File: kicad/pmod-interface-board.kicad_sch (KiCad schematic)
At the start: 30 parts, among them J1 PMOD Connector 1, J2 PMOD Connector 2, J4 Gameboy Cart Connector, U1 74HCT541, U2 74HCT541, U3 74HC595, U4 74HC595, U5 74HC595, U6 74HC597

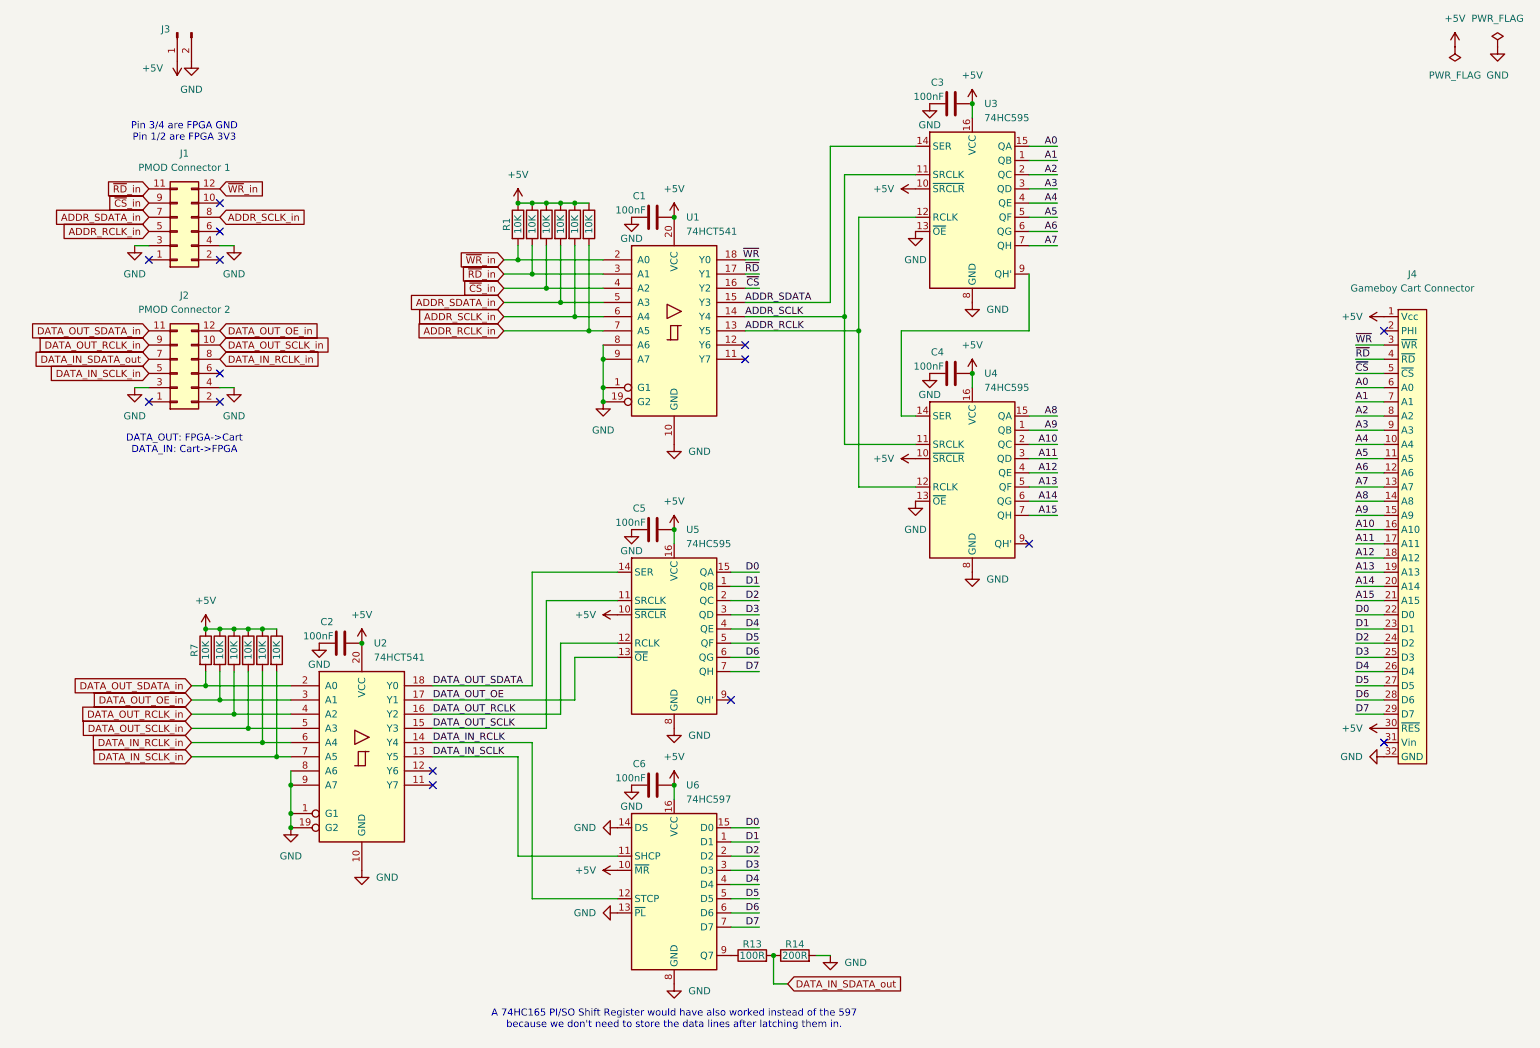
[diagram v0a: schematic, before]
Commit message: kicad: fixed faulty 597 wiring and moved pullups to +3.3v
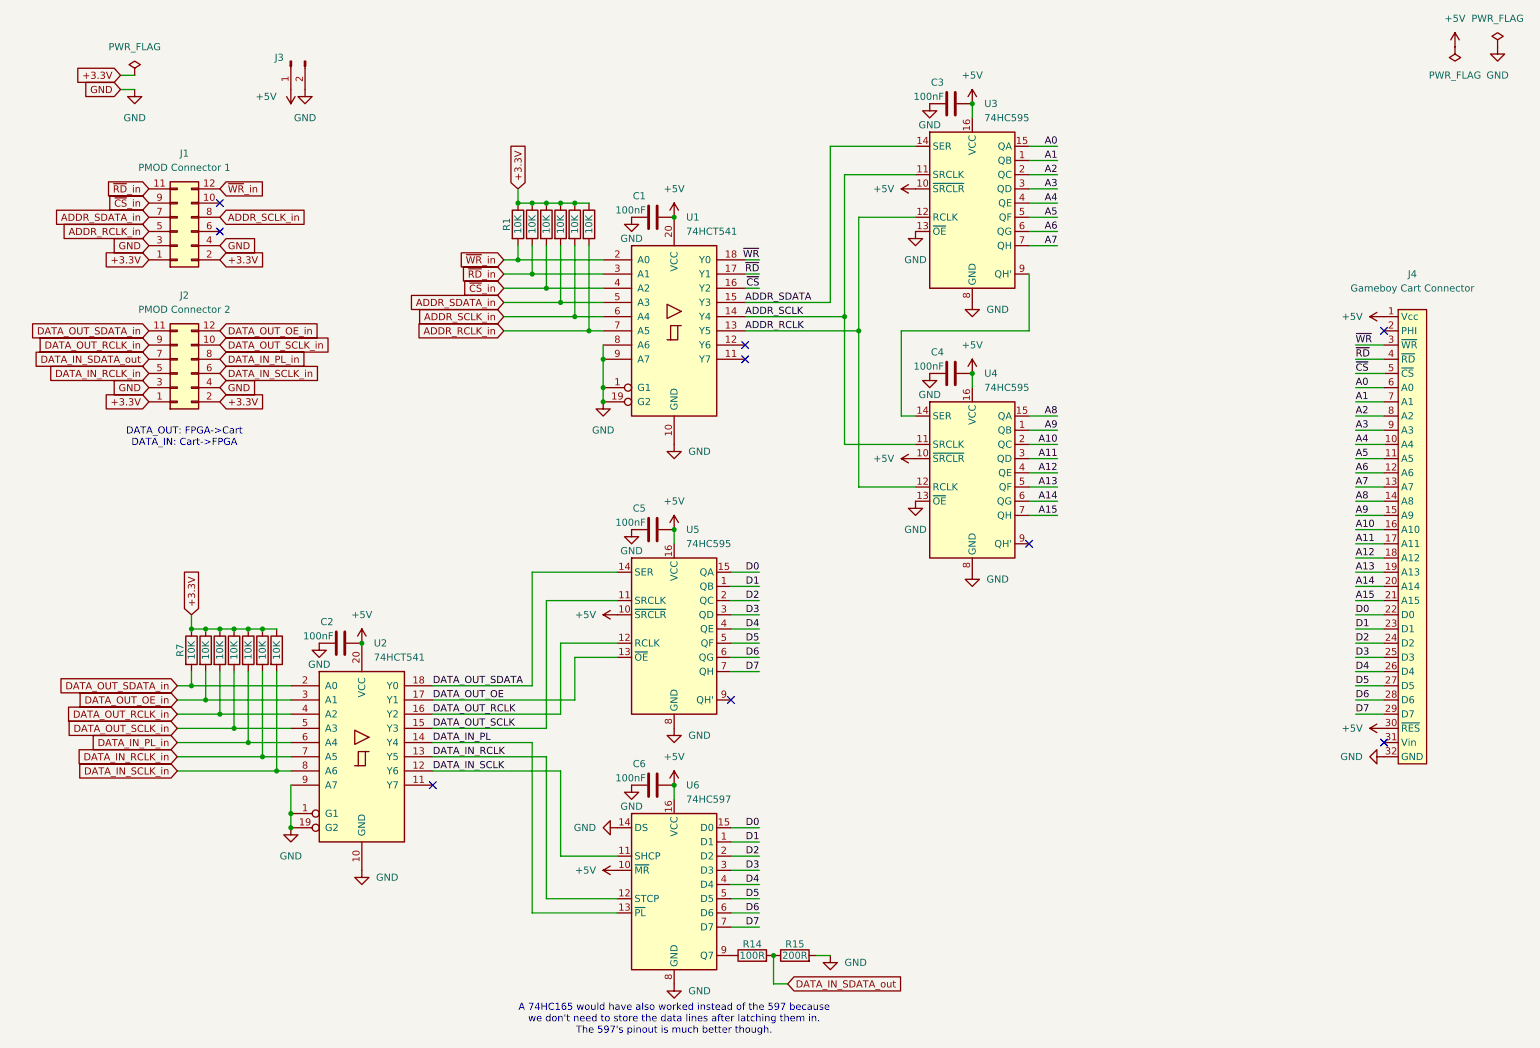
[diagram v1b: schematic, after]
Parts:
- added R13: 10K, Resistor_THT:R_Axial_DIN0204_L3.6mm_D1.6mm_P5.08mm_Horizontal, symbol Device:R
- renumbered R13 to R14, R14 to R15
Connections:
- net +5V: no longer R1.1, R10.1, R11.1, R12.1, R2.1, R3.1, R4.1, R5.1, R6.1, R7.1, R8.1, R9.1
- net DATA_IN_RCLK: now also U2.13 (Y5); no longer U2.14 (Y4)
- net DATA_IN_RCLK_in: now also J2.5 (Pin_5), R12.2, U2.7 (A5); no longer J2.8 (Pin_8), R11.2, U2.6 (A4)
- net DATA_IN_SCLK: now also U2.12 (Y6); no longer U2.13 (Y5)
- net DATA_IN_SCLK_in: now also J2.6 (Pin_6), U2.8 (A6), R13.2; no longer J2.5 (Pin_5), R12.2, U2.7 (A5)
- net GND: no longer U2.8 (A6), U6.13 (~{PL})
- net +3.3V: now reaches J1.1 (Pin_1)
- net +3.3V: now also J1.2 (Pin_2), J2.1 (Pin_1), J2.2 (Pin_2), R1.1, R10.1, R11.1, R12.1, R2.1, R3.1, R4.1, R5.1, R6.1, R7.1, R8.1, R9.1, R13.1
- new net DATA_IN_PL: U2.14 (Y4), U6.13 (~{PL})
- new net DATA_IN_PL_in: J2.8 (Pin_8), R11.2, U2.6 (A4)
- no-connect marks 15 -> 9
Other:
- note added: "A 74HC165 would have also worked instead of the 597 because we don't need to store the data lines after latching them in. The 597's pinout is much better though."
- note removed: "A 74HC165 PI/SO Shift Register would have also worked instead of the 597 because we don't need to store the data lines after latching them in."
- note removed: "Pin 3/4 are FPGA GND Pin 1/2 are FPGA 3V3"
- moved on the sheet: J3, R7

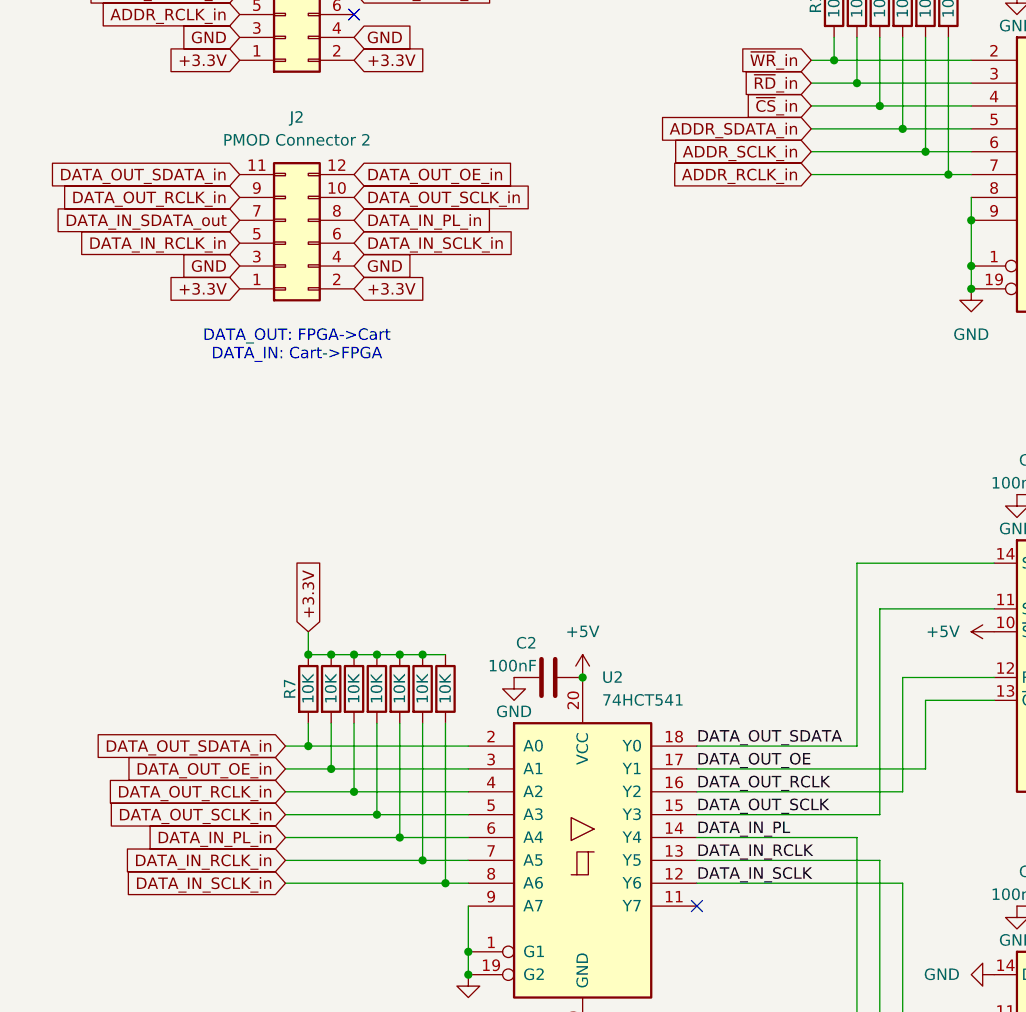
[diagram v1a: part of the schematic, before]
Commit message: src/kicad: fixed incorrectly named OE and PL pins to ~OE and ~PL
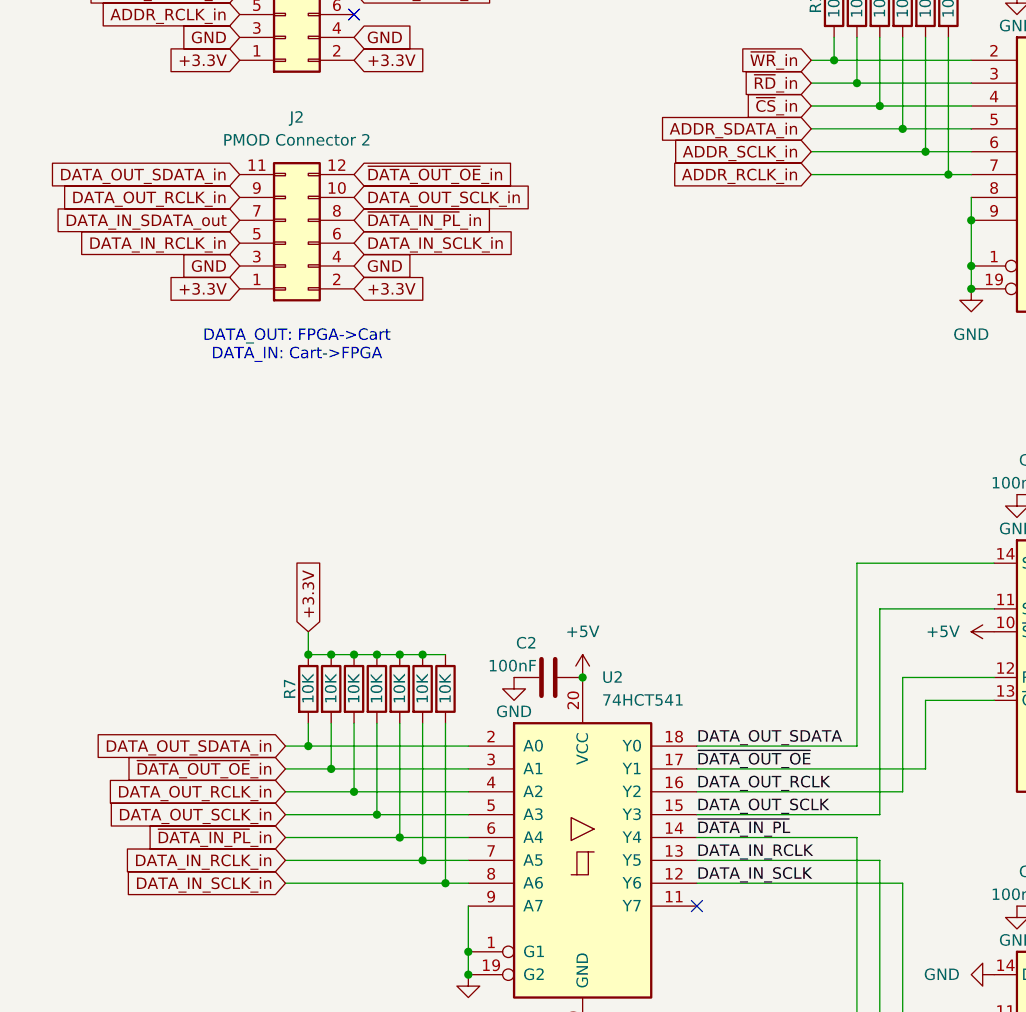
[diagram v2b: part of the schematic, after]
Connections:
- net DATA_IN_PL renamed ~{DATA_IN_PL}
- net DATA_IN_PL_in renamed ~{DATA_IN_PL}_in
- net DATA_OUT_OE renamed ~{DATA_OUT_OE}
- net DATA_OUT_OE_in renamed ~{DATA_OUT_OE}_in
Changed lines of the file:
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@@
 		)
 	)
-	(label "DATA_IN_PL"
+	(label "~{DATA_IN_PL}"
 		(at 86.36 144.78 0)
 		(effects
@@
 		)
 	)
-	(label "DATA_OUT_OE"
+	(label "~{DATA_OUT_OE}"
 		(at 86.36 137.16 0)
 		(effects
@@
 		)
 	)
-	(global_label "DATA_IN_PL_in"
+	(global_label "~{DATA_IN_PL}_in"
 		(shape input)
 		(at 40.64 144.78 180)
@@
 		)
 	)
-	(global_label "DATA_OUT_OE_in"
+	(global_label "~{DATA_OUT_OE}_in"
 		(shape input)
 		(at 48.26 71.12 0)
@@
 		)
 	)
-	(global_label "DATA_OUT_OE_in"
+	(global_label "~{DATA_OUT_OE}_in"
 		(shape input)
 		(at 40.64 137.16 180)
@@
 		)
 	)
-	(global_label "DATA_IN_PL_in"
+	(global_label "~{DATA_IN_PL}_in"
 		(shape input)
 		(at 48.26 76.2 0)
